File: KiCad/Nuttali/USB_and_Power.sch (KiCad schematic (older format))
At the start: 1 part

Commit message: Fixed power and USB
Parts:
- added U?: USBLC6-2P6, Package_TO_SOT_SMD:SOT-666, symbol Power_Protection:USBLC6-2P6
- added U?: AP1117-15, Package_TO_SOT_SMD:SOT-223-3_TabPin2, symbol Regulator_Linear:AP1117-15
- added U?: AP131-15, Package_TO_SOT_SMD:SOT-23-5, symbol Regulator_Linear:AP131-15
- J?: value USB Connector -> B4B-XH-A
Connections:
- net +5V: now reaches J?.1 (Pin_1)
- net +5V: now also U?.2 (GND)
- net at J?.2 (Pin_2): now also U?.1 (I/O1)
- net at J?.3 (Pin_3): now also U?.3 (I/O2)
- net GND: now reaches J?.4 (Pin_4)
- net GND: now also U?.5 (VBUS)
- new net D+: U?.4 (I/O2)
- new net D-: U?.6 (I/O1)
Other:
- moved on the sheet: J?
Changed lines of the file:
@@
 L Connector:Conn_01x04_Male J?
 U 1 1 601D53F8
-P 2450 3050
-F 0 "J?" H 2558 3331 50  0000 C CNN
-F 1 "USB Connector" H 2558 3240 50  0000 C CNN
-F 2 "" H 2450 3050 50  0001 C CNN
-F 3 "~" H 2450 3050 50  0001 C CNN
-	1    2450 3050
+P 1400 1700
+AR Path="/601D53F8" Ref="J?"  Part="1"
+AR Path="/601D470C/601D53F8" Ref="J?"  Part="1"
+F 0 "J?" H 1508 1981 50  0000 C CNN
+F 1 "B4B-XH-A" H 1508 1890 50  0000 C CNN
+F 2 "" H 1400 1700 50  0001 C CNN
+F 3 "~" H 1400 1700 50  0001 C CNN
+	1    1400 1700
 	1    0    0    -1
 $EndComp
+$Comp
+L power:+5V #PWR?
+U 1 1 6025442C
+P 1850 1500
+F 0 "#PWR?" H 1850 1350 50  0001 C CNN
+F 1 "+5V" H 1865 1673 50  0000 C CNN
+F 2 "" H 1850 1500 50  0001 C CNN
+F 3 "" H 1850 1500 50  0001 C CNN
+	1    1850 1500
+	1    0    0    -1
+$EndComp
+Wire Wire Line
+	1600 1600 1850 1600
+Wire Wire Line
+	1850 1600 1850 1500
+$Comp
+L Power_Protection:USBLC6-2P6 U?
+U 1 1 60257671
+P 2550 1800
+F 0 "U?" V 2200 2400 50  0000 C CNN
+F 1 "USBLC6-2P6" V 2300 2400 50  0000 C CNN
+F 2 "Package_TO_SOT_SMD:SOT-666" H 2550 1300 50  0001 C CNN
+F 3 "https://www.st.com/resource/en/datasheet/usblc6-2.pdf" H 2750 2150 50  0001 C CNN
+	1    2550 1800
+	0    1    1    0
+$EndComp
+Wire Wire Line
+	1600 1700 2050 1700
+Wire Wire Line
+	2050 1700 2050 1350
+Wire Wire Line
+	2050 1350 2450 1350
+Wire Wire Line
+	2450 1350 2450 1400
+Wire Wire Line
+	1600 1800 2050 1800
+Wire Wire Line
+	2050 1800 2050 2250
+Wire Wire Line
+	2050 2250 2450 2250
+Wire Wire Line
+	2450 2250 2450 2200
+$Comp
+L power:+5V #PWR?
+U 1 1 60263555
+P 2150 1700
+F 0 "#PWR?" H 2150 1550 50  0001 C CNN
+F 1 "+5V" H 2165 1873 50  0000 C CNN
+F 2 "" H 2150 1700 50  0001 C CNN
+F 3 "" H 2150 1700 50  0001 C CNN
+	1    2150 1700
+	1    0    0    -1
+$EndComp
+Wire Wire Line
+	2150 1800 2150 1700
+Wire Wire Line
+	1600 1900 1850 1900
+$Comp
+L power:GND #PWR?
+U 1 1 60263C21
+P 1850 1900
+F 0 "#PWR?" H 1850 1650 50  0001 C CNN
+F 1 "GND" H 1855 1727 50  0000 C CNN
+F 2 "" H 1850 1900 50  0001 C CNN
+F 3 "" H 1850 1900 50  0001 C CNN
+	1    1850 1900
+	1    0    0    -1
+$EndComp
+Wire Wire Line
+	2950 1800 3000 1800
+$Comp
+L power:GND #PWR?
+U 1 1 6026528C
+P 3000 1800
+F 0 "#PWR?" H 3000 1550 50  0001 C CNN
+F 1 "GND" H 3005 1627 50  0000 C CNN
+F 2 "" H 3000 1800 50  0001 C CNN
+F 3 "" H 3000 1800 50  0001 C CNN
+	1    3000 1800
+	1    0    0    -1
+$EndComp
+Text GLabel 2800 1350 2    50   BiDi ~ 0
+D-
+Text GLabel 2800 2250 2    50   BiDi ~ 0
+D+
+Wire Wire Line
+	2800 1350 2650 1350
+Wire Wire Line
+	2650 1350 2650 1400
+Wire Wire Line
+	2800 2250 2650 2250
+Wire Wire Line
+	2650 2250 2650 2200
+$Comp
+L Regulator_Linear:AP1117-15 U?
+U 1 1 60275CC9
+P 4650 1650
+F 0 "U?" H 4650 1892 50  0000 C CNN
+F 1 "AP1117-15" H 4650 1801 50  0000 C CNN
+F 2 "Package_TO_SOT_SMD:SOT-223-3_TabPin2" H 4650 1850 50  0001 C CNN
+F 3 "http://www.diodes.com/datasheets/AP1117.pdf" H 4750 1400 50  0001 C CNN
+	1    4650 1650
+	1    0    0    -1
+$EndComp
+$Comp
+L Regulator_Linear:AP131-15 U?
+U 1 1 602779E7
+P 4650 2650
+F 0 "U?" H 4650 2992 50  0000 C CNN
+F 1 "AP131-15" H 4650 2901 50  0000 C CNN
+F 2 "Package_TO_SOT_SMD:SOT-23-5" H 4650 2975 50  0001 C CNN
+F 3 "http://www.diodes.com/_files/datasheets/AP131.pdf" H 4650 2650 50  0001 C CNN
+	1    4650 2650
+	1    0    0    -1
+$EndComp

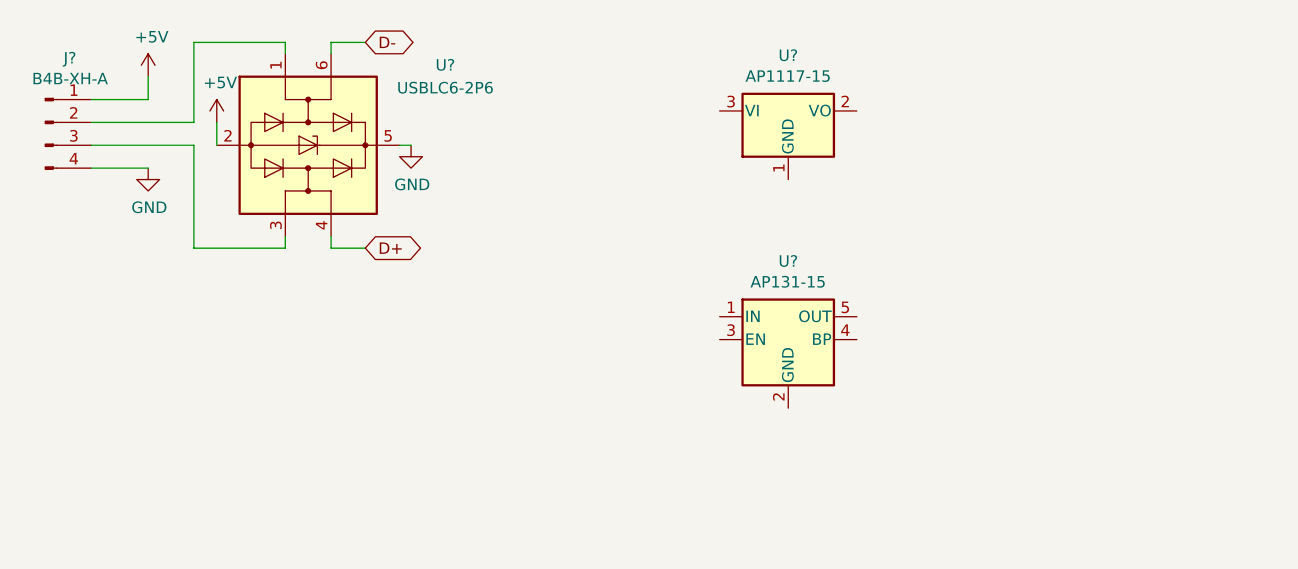
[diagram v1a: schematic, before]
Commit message: Fixed power and usb
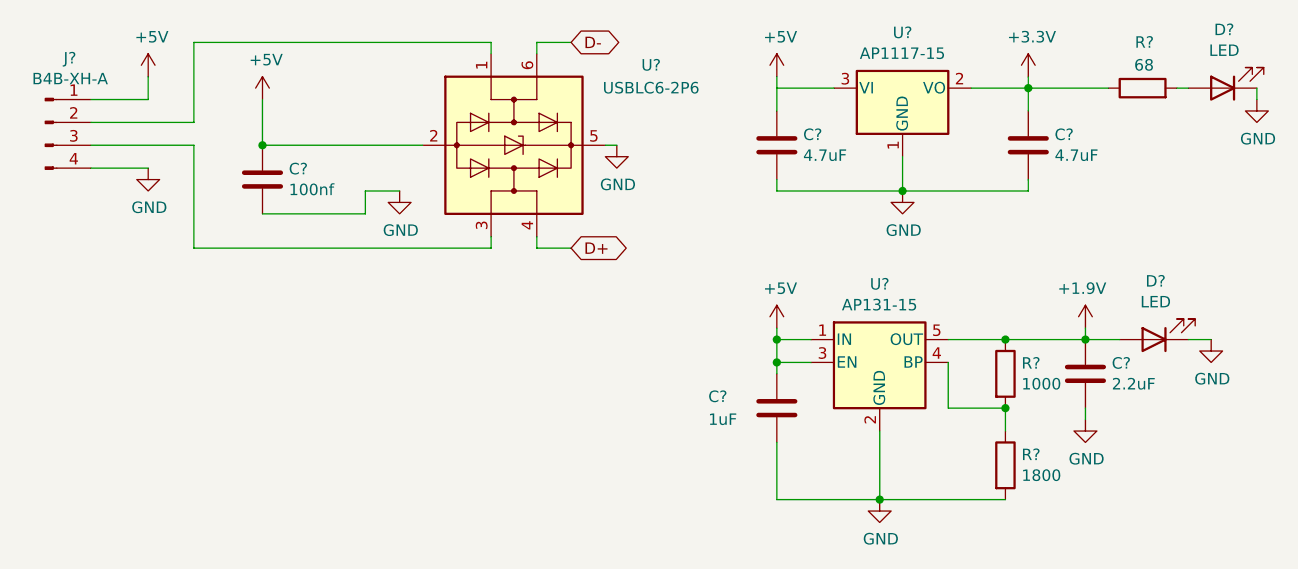
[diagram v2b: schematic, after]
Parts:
- added C?: 100nf, symbol Device:C
- added C? (x2): 4.7uF, symbol Device:C
- added C?: 1uF, symbol Device:C
- added C?: 2.2uF, symbol Device:C
- added D? (x2): LED, symbol Device:LED
- added R?: 1000, symbol Device:R
- added R?: 1800, symbol Device:R
- added R?: 68, symbol Device:R
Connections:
- net +5V: now also U?.1 (IN), U?.3 (EN), U?.3 (VI), C?.1, C?.1, C?.1
- net GND: now also U?.1 (GND), U?.2 (GND), C?.2, C?.2, C?.2, C?.2, C?.2, D?.1 (K), D?.1 (K), R?.2
- net +3V3: now reaches U?.2 (VO)
- net +3V3: now also C?.1, R?.1
- net at U?.4 (BP): now also R?.1, R?.2
- net +1V0: now reaches U?.5 (OUT)
- net +1V0: now also C?.1, D?.2 (A), R?.1
- new net: D?.2 (A), R?.2
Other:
- moved on the sheet: U?
